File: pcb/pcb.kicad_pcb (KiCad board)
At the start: 2 copper layers, 137.5 x 93.4 mm, 51 parts, among them SW1 SW_SPST, SW10 SW_SPST, SW11 SW_SPST, SW12 SW_SPST, SW13 SW_SPST, SW14 SW_SPST, SW15 SW_SPST, SW16 SW_SPST, SW17 SW_SPST, SW18 SW_SPST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

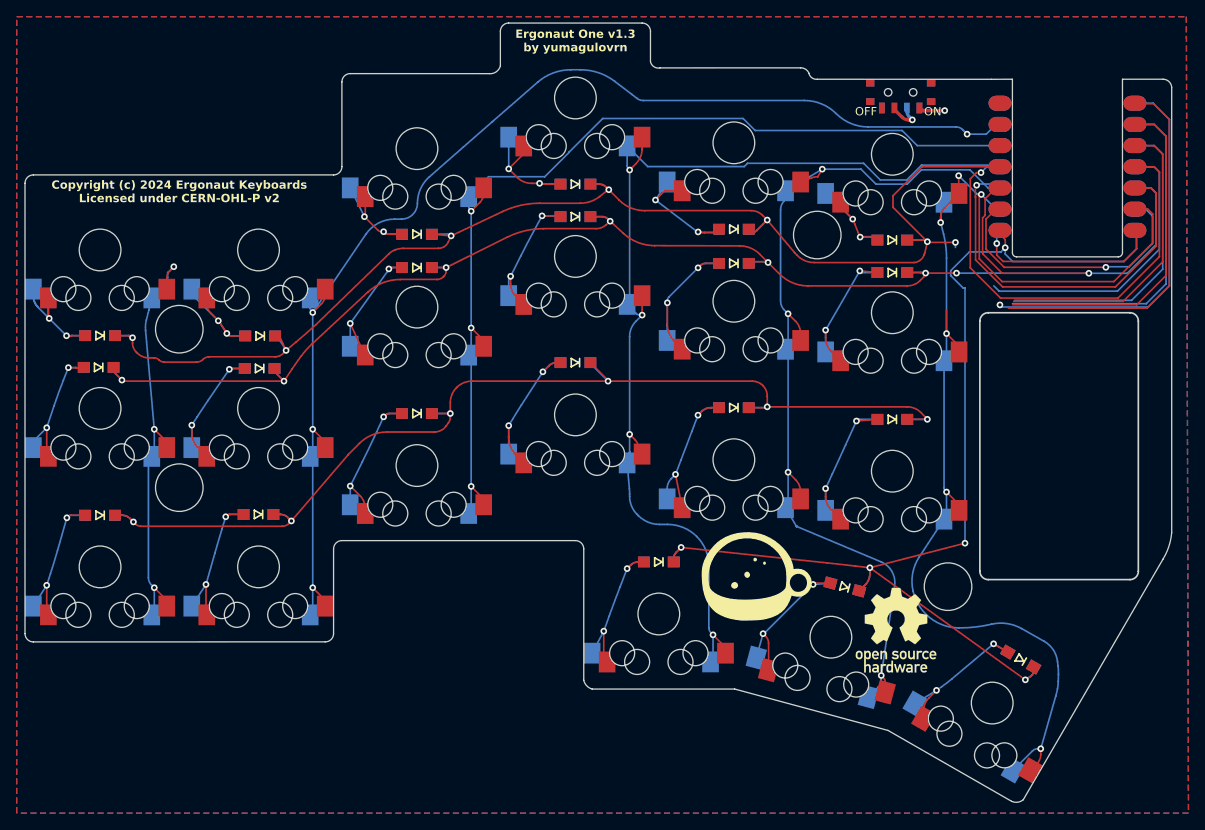
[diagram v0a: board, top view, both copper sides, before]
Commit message: Дорожки развёл
вокруг окна
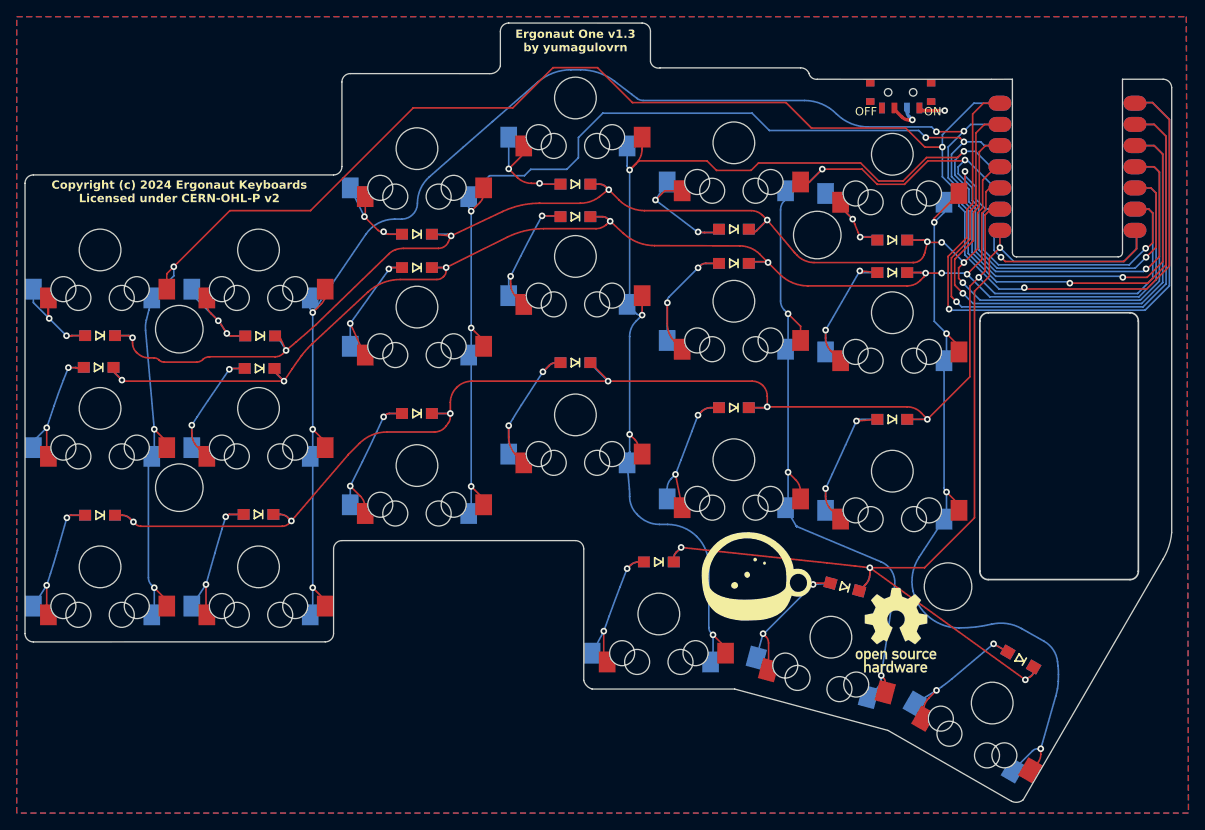
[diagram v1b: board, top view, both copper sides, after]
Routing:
- net C0: track 93.6 -> 228.0 mm, vias 3 -> 5
- net unconnected-(U1-5V-Pad14): track 45.9 -> 80.2 mm
- net GND: track 40.9 -> 72.6 mm, vias 0 -> 1
- net unconnected-(U1-3V3-Pad12)_1: track 36.4 -> 65.1 mm, vias 0 -> 1
- net R2: track 169.8 -> 198.3 mm
- net C2: track 148.4 -> 170.3 mm, vias 3 -> 6
- net C1: track 181.5 -> 202.8 mm, vias 4 -> 6
- net R1: track 190.8 -> 185.5 mm
- net R3: track 133.9 -> 129.6 mm, vias 5 -> 4
- net R0: track 197.2 -> 200.6 mm, vias 7 -> 9
- net C4: track 151.6 -> 154.7 mm, vias 5 -> 6
- net C3: track 178.8 -> 176.5 mm, vias 5 -> 6
- net Net-(D1-A): track 17.4 -> 16.8 mm

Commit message: красоту навёл
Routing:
- net C1: track 202.8 -> 205.6 mm
- net unconnected-(U1-3V3-Pad12)_1: track 65.1 -> 63.9 mm
- net R2: track 198.3 -> 197.1 mm
- net R0: track 200.6 -> 199.5 mm, vias 9 -> 8
- net C5: track 142.1 -> 141.0 mm
- net GND: track 72.6 -> 71.6 mm
- net R1: track 185.5 -> 184.6 mm, vias 8 -> 7
- net unconnected-(U1-5V-Pad14): track 80.2 -> 79.3 mm

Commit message: Выровнял по Z
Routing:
- net C5: track 141.0 -> 136.8 mm
- net R2: track 197.1 -> 195.9 mm
- net R3: track 129.6 -> 128.5 mm
- net C4: track 154.3 -> 153.4 mm
- net C3: track 176.5 -> 175.6 mm
- net unconnected-(U1-B8_TX/1.11-Pad7)_1: track 23.2 -> 22.4 mm
- net R1: track 184.6 -> 183.9 mm

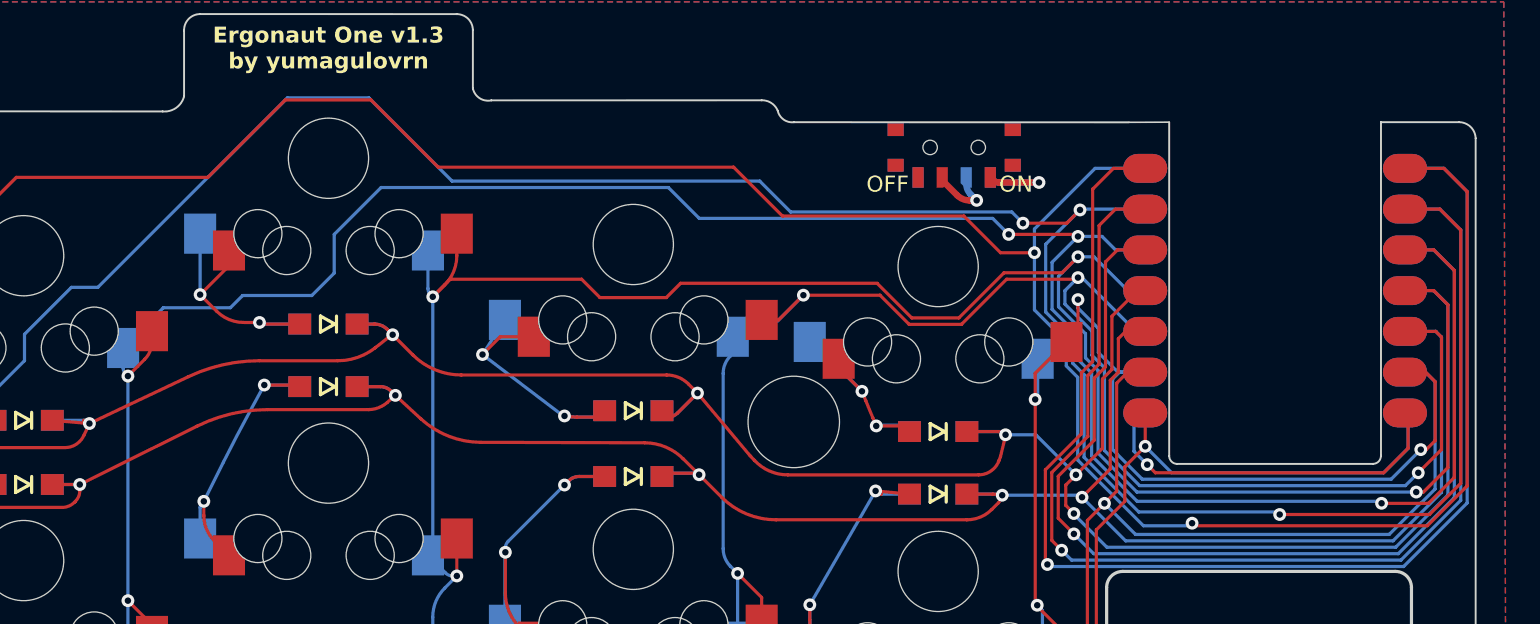
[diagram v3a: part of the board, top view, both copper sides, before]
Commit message: расширил вырез
и добавил пады питания
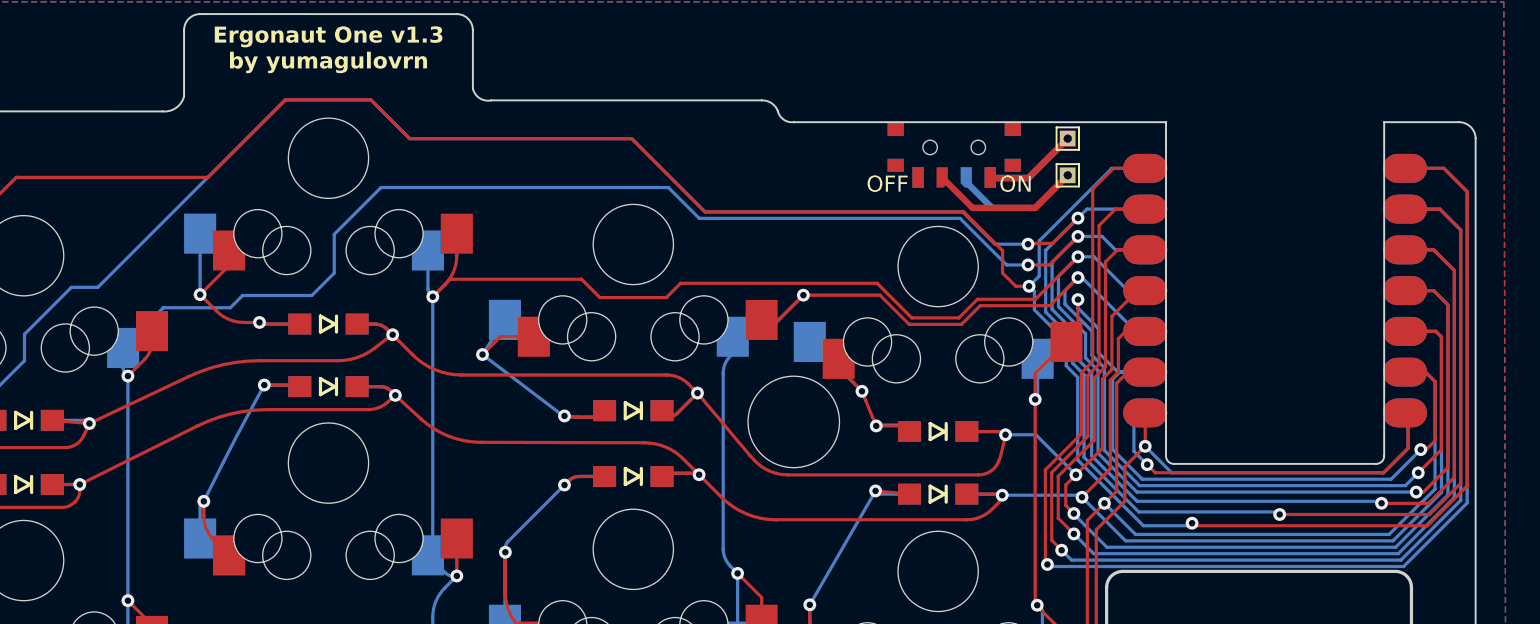
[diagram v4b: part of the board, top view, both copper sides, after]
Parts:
- added H5: 19, TestPoint:TestPoint_THTPad_1.0x1.0mm_Drill0.5mm, F.Cu at (187.6, 56.6)
- added H6: BAT+, TestPoint:TestPoint_THTPad_1.0x1.0mm_Drill0.5mm, F.Cu at (187.6, 58.9)
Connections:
- PWR1 pad 1: B+ -> Net-(PWR1-A)
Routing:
- net unconnected-(U1-5V-Pad14)_1: track 79.3 -> 0.00 mm, vias 1 -> 0
- net unconnected-(U1-5V-Pad14): track 0.00 -> 79.3 mm, vias 0 -> 1
- net unconnected-(U1-3V3-Pad12)_1: track 0.00 -> 63.9 mm, vias 0 -> 1
- net unconnected-(U1-3V3-Pad12): track 63.9 -> 0.00 mm, vias 1 -> 0
- net unconnected-(U1-B8_TX/1.11-Pad7)_1: track 0.00 -> 22.4 mm, vias 0 -> 1
- net unconnected-(U1-B8_TX/1.11-Pad7): track 22.4 -> 0.00 mm, vias 1 -> 0
- net Net-(PWR1-B): track 3.79 -> 17.6 mm, vias 1 -> 0
- net Net-(PWR1-A): track 0.00 -> 12.2 mm
- net B+: track 6.28 -> 0.00 mm, vias 1 -> 0
- net C2: track 170.2 -> 171.7 mm
- net C0: track 227.9 -> 228.9 mm
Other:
- outline, holes or cut-outs redrawn

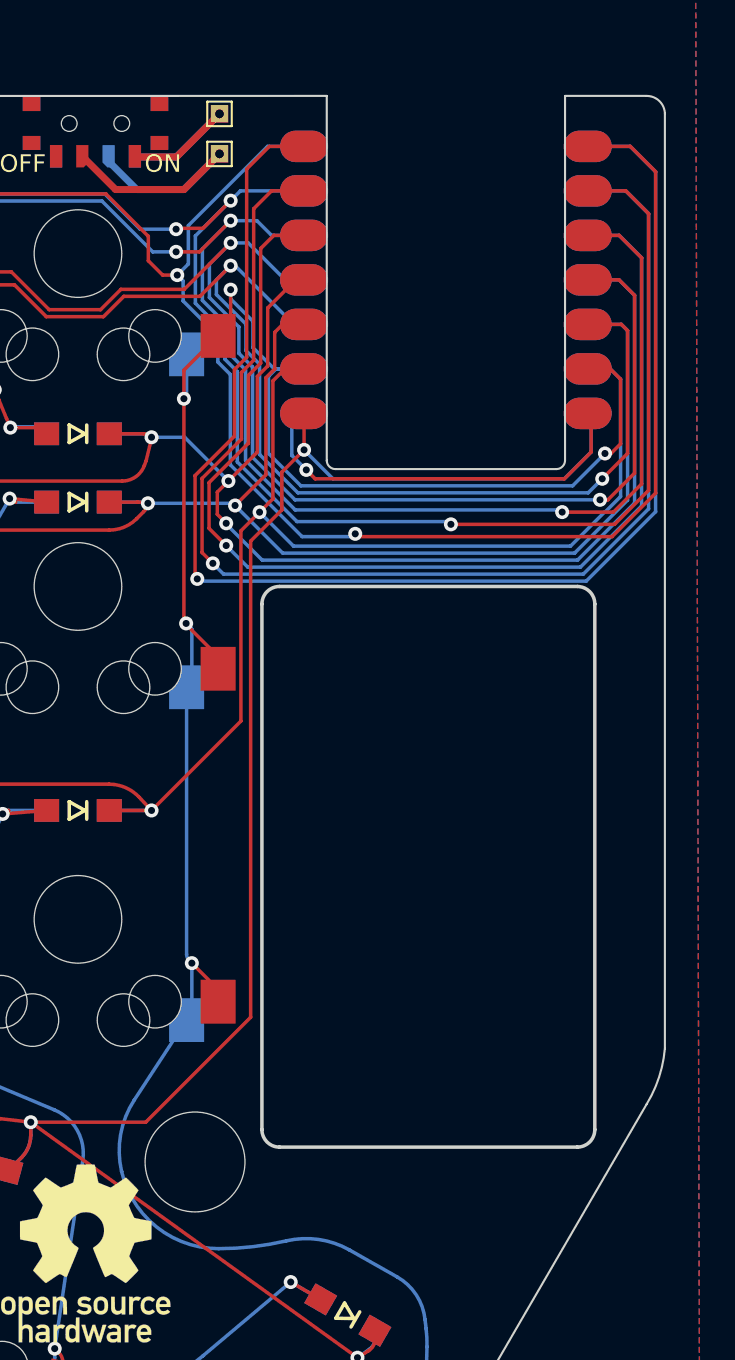
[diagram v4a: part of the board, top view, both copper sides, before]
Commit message: добавил батарейку
и разъём с другой стороны
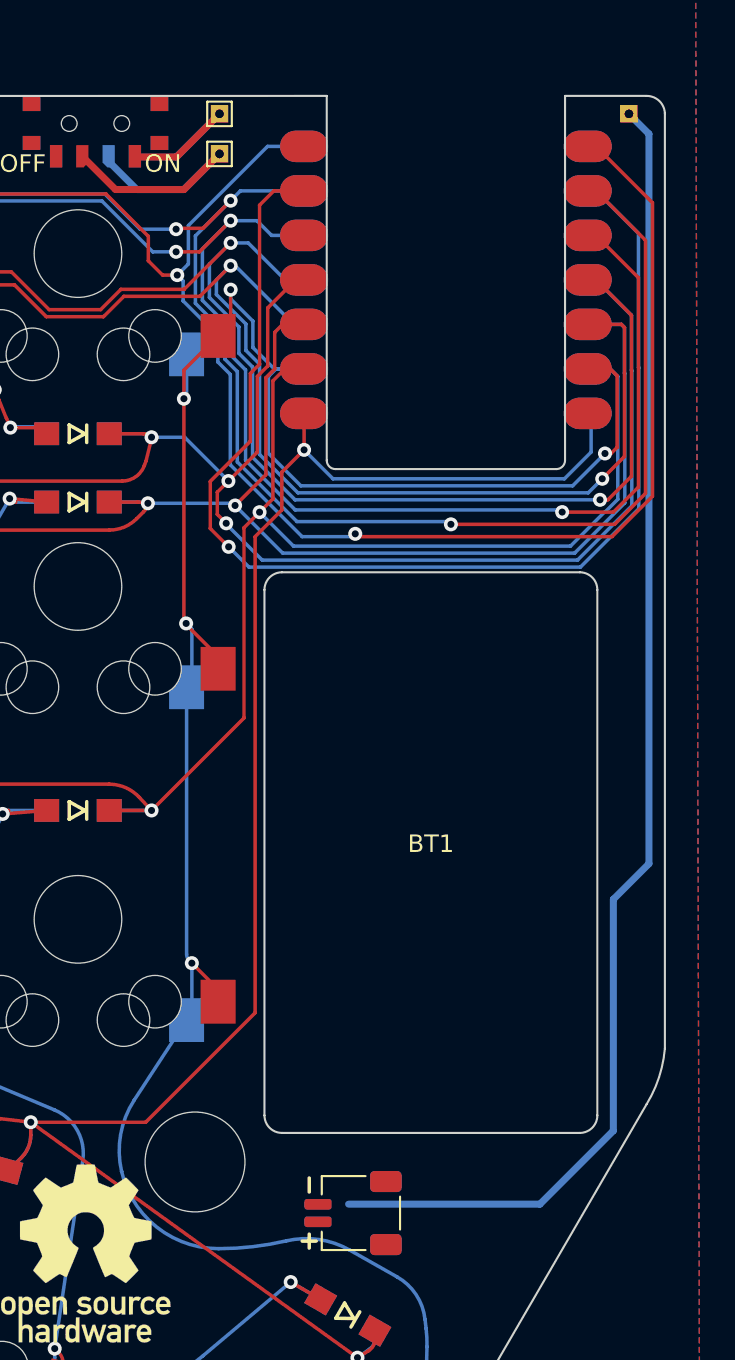
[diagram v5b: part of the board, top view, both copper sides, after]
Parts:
- added ?: , , F.Cu at (210.9, 56.6)
- added BT1: LP601730, Two:lp601730, F.Cu at (199.6, 98.8)
- added J1: Conn_01x02_Pin, Two:JST_SH_Battery_DUAL_, F.Cu at (195.2, 119.4)
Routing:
- net unconnected-(U1-5V-Pad14): track 79.3 -> 0.00 mm, vias 1 -> 0
- net (no net): track 0.00 -> 76.2 mm
- net unconnected-(U1-3V3-Pad12)_1: track 63.9 -> 0.00 mm, vias 1 -> 0
- net unconnected-(U1-B8_TX/1.11-Pad7)_1: track 22.4 -> 0.00 mm, vias 1 -> 0
- net GND: track 71.6 -> 67.9 mm
- net C0: track 228.9 -> 227.6 mm
- net C1: track 206.0 -> 204.9 mm
- net C2: track 171.7 -> 170.8 mm
- net C3: track 175.6 -> 174.7 mm
- net R0: track 199.5 -> 198.6 mm
- net Net-(PWR1-A): track 12.2 -> 11.6 mm
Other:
- outline, holes or cut-outs redrawn

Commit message: in progress
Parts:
- removed ?: , 
- removed H5: 19, TestPoint:TestPoint_THTPad_1.0x1.0mm_Drill0.5mm
- removed H6: BAT+, TestPoint:TestPoint_THTPad_1.0x1.0mm_Drill0.5mm
- removed J1: Conn_01x02_Pin, Two:JST_SH_Battery_DUAL_
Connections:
- PWR1 pad 2: Net-(PWR1-B) -> Net-(BT1-+)
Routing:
- net Net-(BT1-+): track 0.00 -> 100.5 mm, vias 0 -> 2
- net (no net): track 76.2 -> 0.00 mm
- net Net-(BT1--): track 0.00 -> 67.4 mm
- net Net-(PWR1-B): track 17.3 -> 0.00 mm
- net Net-(PWR1-A): track 11.6 -> 16.5 mm
- net C5: track 136.6 -> 132.8 mm
- net C0: track 227.6 -> 229.8 mm
- net R0: track 198.6 -> 199.6 mm
- net C4: track 153.3 -> 152.4 mm
- net C3: track 174.7 -> 175.2 mm
- net R2: track 195.8 -> 196.3 mm
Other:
- outline, holes or cut-outs redrawn
